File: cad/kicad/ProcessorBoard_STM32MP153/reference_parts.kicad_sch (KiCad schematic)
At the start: 25 parts, among them Q99901 MMBT5551L, Q99902 MMBTA92, SW99901 SW_DIP_x03

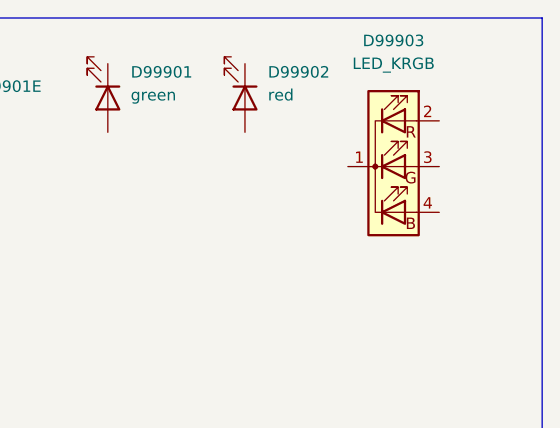
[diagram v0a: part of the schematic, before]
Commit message: double inversion trap
the crab has a double inversion, the pins internal logic is inverted. and the output logic-high is dynamically determined. bruh
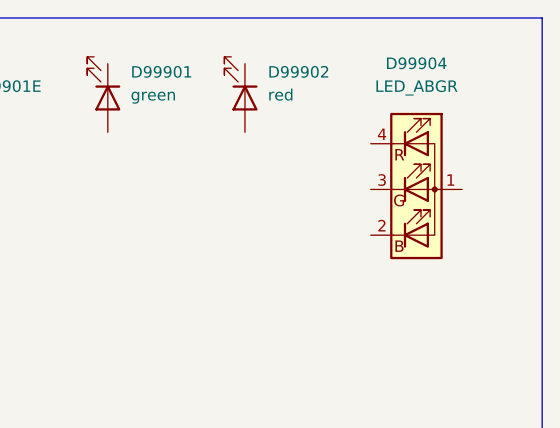
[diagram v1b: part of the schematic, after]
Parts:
- removed D99903: LED_KRGB, LED_SMD:LED_Cree-PLCC4_2x2mm_CW, symbol Device:LED_KRGB
- added D99904: LED_ABGR, symbol Device:LED_ABGR
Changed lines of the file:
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@@
+	)
+	(symbol
+		(lib_id "Device:LED_ABGR")
+		(at 194.31 33.02 0)
+		(unit 1)
+		(body_style 1)
+		(exclude_from_sim no)
+		(in_bom yes)
+		(on_board yes)
+		(in_pos_files yes)
+		(dnp no)
+		(fields_autoplaced yes)
+		(property "Reference" "D99904"
+			(at 194.31 19.05 0)
+			(show_name no)
+			(do_not_autoplace no)
+			(effects
+				(font
+					(size 1.27 1.27)
+				)
+			)
+		)
+		(property "Value" "LED_ABGR"
+			(at 194.31 21.59 0)
+			(show_name no)
+			(do_not_autoplace no)
+			(effects
+				(font
+					(size 1.27 1.27)
+				)
+			)
+		)
+		(property "Footprint" ""
+			(at 194.31 34.29 0)
+			(hide yes)
+			(show_name no)
+			(do_not_autoplace no)
+			(effects
+				(font
+					(size 1.27 1.27)
+				)
+			)
+		)
+		(property "Datasheet" "https://downloads.cree-led.com/files/ds/h/HB-CLMVH-FKA.pdf"
+			(at 194.31 34.29 0)
+			(hide yes)
+			(show_name no)
+			(do_not_autoplace no)
+			(effects
+				(font
+					(size 1.27 1.27)
+				)
+			)
+		)
+		(property "Description" "RGB LED, com-anode, red/green/blue"
+			(at 194.31 33.02 0)
+			(hide yes)
+			(show_name no)
+			(do_not_autoplace no)
+			(effects
+				(font
+					(size 1.27 1.27)
+				)
+			)
+		)
+		(property "mouser" "https://www.mouser.com/en/ProductDetail/Cree-LED/CLMVH-FKA-V3E27C3M2RMG6EB4B3?qs=vcFyY%252BOcAyjw5C6eEBWdHQ%3D%3D"
+			(at 194.31 33.02 0)
+			(hide yes)
+			(show_name no)
+			(do_not_autoplace no)
+			(effects
+				(font
+					(size 1.27 1.27)
+				)
+			)
+		)
+		(property "unit x1" "0.10"
+			(at 194.31 33.02 0)
+			(hide yes)
+			(show_name no)
+			(do_not_autoplace no)
+			(effects
+				(font
+					(size 1.27 1.27)
+				)
+			)
+		)
+		(property "unit x10" "0.007"
+			(at 194.31 33.02 0)
+			(hide yes)
+			(show_name no)
+			(do_not_autoplace no)
+			(effects
+				(font
+					(size 1.27 1.27)
+				)
+			)
+		)
+		(pin "2"
+		)
+		(pin "1"
+		)
+		(pin "4"
+		)
+		(pin "3"
+		)
+		(instances
+			(project "ProcessorBoard_STM32MP153"
+				(path "/e63e39d7-6ac0-4ffd-8aa3-1841a4541b55/157228c5-c462-4e2c-89a8-acc0a1fe94b2"
+					(reference "D99904")
+					(unit 1)
+				)
+			)
+		)
 	)
 	(symbol
@@
 					(unit 1)
 				)
-			)
-		)
-	)
-	(symbol
-		(lib_id "Device:LED_KRGB")
-		(at 191.77 30.48 0)
-		(unit 1)
-		(body_style 1)
-		(exclude_from_sim no)
-		(in_bom yes)
-		(on_board yes)
-		(in_pos_files yes)
-		(dnp no)
-		(fields_autoplaced yes)
-		(property "Reference" "D99903"
-			(at 191.77 16.51 0)
-			(show_name no)
-			(do_not_autoplace no)
-			(effects
-				(font
-					(size 1.27 1.27)
-				)
-			)
-		)
-		(property "Value" "LED_KRGB"
-			(at 191.77 19.05 0)
-			(show_name no)
-			(do_not_autoplace no)
-			(effects
-				(font
-					(size 1.27 1.27)
-				)
-			)
-		)
-		(property "Footprint" "LED_SMD:LED_Cree-PLCC4_2x2mm_CW"
-			(at 191.77 31.75 0)
-			(hide yes)
-			(show_name no)
-			(do_not_autoplace no)
-			(effects
-				(font
-					(size 1.27 1.27)
-				)
-			)
-		)
-		(property "Datasheet" "https://downloads.cree-led.com/files/ds/h/HB-CLMVH-FKA.pdf"
-			(at 191.77 31.75 0)
-			(hide yes)
-			(show_name no)
-			(do_not_autoplace no)
-			(effects
-				(font
-					(size 1.27 1.27)
-				)
-			)
-		)
-		(property "Description" "RGB LED, cathode/red/green/blue"
-			(at 191.77 30.48 0)
-			(hide yes)
-			(show_name no)
-			(do_not_autoplace no)
-			(effects
-				(font
-					(size 1.27 1.27)
-				)
-			)
-		)
-		(property "mouser" "https://www.mouser.com/en/ProductDetail/Cree-LED/CLMVH-FKA-V3E27C3M2RMG6EB4B3?qs=vcFyY%252BOcAyjw5C6eEBWdHQ%3D%3D"
-			(at 191.77 30.48 0)
-			(hide yes)
-			(show_name no)
-			(do_not_autoplace no)
-			(effects
-				(font
-					(size 1.27 1.27)
-				)
-			)
-		)
-		(property "unit x1" "0.10"
-			(at 191.77 30.48 0)
-			(hide yes)
-			(show_name no)
-			(do_not_autoplace no)
-			(effects
-				(font
-					(size 1.27 1.27)
-				)
-			)
-		)
-		(property "unit x10" "0.007"
-			(at 191.77 30.48 0)
-			(hide yes)
-			(show_name no)
-			(do_not_autoplace no)
-			(effects
-				(font
-					(size 1.27 1.27)
-				)
-			)
-		)
-		(pin "1"
-		)
-		(pin "3"
-		)
-		(pin "2"
-		)
-		(pin "4"
-		)
-		(instances
-			(project "ProcessorBoard_STM32MP153"
-				(path "/e63e39d7-6ac0-4ffd-8aa3-1841a4541b55/157228c5-c462-4e2c-89a8-acc0a1fe94b2"
-					(reference "D99903")
-					(unit 1)
-				)

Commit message: all hail the auto router
https://ih1.redbubble.net/image.6083290940.2638/flat,750x,075,f-pad,750x1000,f8f8f8.jpg
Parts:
- C903, C904, C905: footprint Capacitor_SMD:C_01005_0402Metric_Pad0.57x0.30mm_HandSolder -> Capacitor_SMD:C_0402_1005Metric_Pad0.74x0.62mm_HandSolder

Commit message: somewhat fanned
the auto router sucks :( . and the auto fanout sucks. and i routed everything on the wrong grid and it snapped to teh wrong places and i only noticed most of teh way though so i push and make it tomorrows problem
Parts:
- renumbered C901 to C99901, C903 to C99902, C902 to C99903, C904 to C99904, C906 to C99905, C905 to C99906, D99904 to D99903, L901 to L99901, L99901 to L99902, R904 to R99901, R99901 to R99902, R99902 to R99903, R905 to R99904, R99903 to R99905, R901 to R99906, R903 to R99907, R906 to R99908, R99904 to R99909, R907 to R99910
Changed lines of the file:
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@@
 		(dnp no)
 		(fields_autoplaced yes)
-		(property "Reference" "C906"
+		(property "Reference" "C99905"
 			(at 92.71 88.9062 0)
 			(show_name no)
@@
 			(project "ProcessorBoard_STM32MP153"
 				(path "/e63e39d7-6ac0-4ffd-8aa3-1841a4541b55/157228c5-c462-4e2c-89a8-acc0a1fe94b2"
-					(reference "C906")
+					(reference "C99905")
 					(unit 1)
 				)
@@
 		(dnp no)
 		(fields_autoplaced yes)
-		(property "Reference" "R99904"
+		(property "Reference" "R99909"
 			(at 87.63 19.0499 0)
 			(show_name no)
@@
 			(project "ProcessorBoard_STM32MP153"
 				(path "/e63e39d7-6ac0-4ffd-8aa3-1841a4541b55/157228c5-c462-4e2c-89a8-acc0a1fe94b2"
-					(reference "R99904")
+					(reference "R99909")
 					(unit 1)
 				)
@@
 		(dnp no)
 		(fields_autoplaced yes)
-		(property "Reference" "R99901"
+		(property "Reference" "R99902"
 			(at 21.59 19.0499 0)
 			(show_name no)
@@
 			(project "ProcessorBoard_STM32MP153"
 				(path "/e63e39d7-6ac0-4ffd-8aa3-1841a4541b55/157228c5-c462-4e2c-89a8-acc0a1fe94b2"
-					(reference "R99901")
+					(reference "R99902")
 					(unit 1)
 				)
@@
 		(dnp no)
 		(fields_autoplaced yes)
-		(property "Reference" "R901"
+		(property "Reference" "R99906"
 			(at 55.88 19.0499 0)
 			(show_name no)
@@
 			(project "ProcessorBoard_STM32MP153"
 				(path "/e63e39d7-6ac0-4ffd-8aa3-1841a4541b55/157228c5-c462-4e2c-89a8-acc0a1fe94b2"
-					(reference "R901")
+					(reference "R99906")
 					(unit 1)
 				)
@@
 		(dnp no)
 		(fields_autoplaced yes)
-		(property "Reference" "C904"
+		(property "Reference" "C99904"
 			(at 82.55 88.9062 0)
 			(show_name no)
@@
 			(project "ProcessorBoard_STM32MP153"
 				(path "/e63e39d7-6ac0-4ffd-8aa3-1841a4541b55/157228c5-c462-4e2c-89a8-acc0a1fe94b2"
-					(reference "C904")
+					(reference "C99904")
 					(unit 1)
 				)
@@
 		(dnp no)
 		(fields_autoplaced yes)
-		(property "Reference" "L901"
+		(property "Reference" "L99901"
 			(at 20.32 121.9199 0)
 			(show_name no)
@@
 			(project "ProcessorBoard_STM32MP153"
 				(path "/e63e39d7-6ac0-4ffd-8aa3-1841a4541b55/157228c5-c462-4e2c-89a8-acc0a1fe94b2"
-					(reference "L901")
+					(reference "L99901")
 					(unit 1)
 				)
@@
 		(dnp no)
 		(fields_autoplaced yes)
-		(property "Reference" "C905"
+		(property "Reference" "C99906"
 			(at 102.87 88.9062 0)
 			(show_name no)
@@
 			(project "ProcessorBoard_STM32MP153"
 				(path "/e63e39d7-6ac0-4ffd-8aa3-1841a4541b55/157228c5-c462-4e2c-89a8-acc0a1fe94b2"
-					(reference "C905")
+					(reference "C99906")
 					(unit 1)
 				)
@@
 		(dnp no)
 		(fields_autoplaced yes)
-		(property "Reference" "D99904"
+		(property "Reference" "D99903"
 			(at 194.31 19.05 0)
 			(show_name no)
@@
 			(project "ProcessorBoard_STM32MP153"
 				(path "/e63e39d7-6ac0-4ffd-8aa3-1841a4541b55/157228c5-c462-4e2c-89a8-acc0a1fe94b2"
-					(reference "D99904")
+					(reference "D99903")
 					(unit 1)
 				)
@@
 		(dnp no)
 		(fields_autoplaced yes)
-		(property "Reference" "R906"
+		(property "Reference" "R99908"
 			(at 76.2 19.0499 0)
 			(show_name no)
@@
 			(project "ProcessorBoard_STM32MP153"
 				(path "/e63e39d7-6ac0-4ffd-8aa3-1841a4541b55/157228c5-c462-4e2c-89a8-acc0a1fe94b2"
-					(reference "R906")
+					(reference "R99908")
 					(unit 1)
 				)
@@
 		(dnp no)
 		(fields_autoplaced yes)
-		(property "Reference" "C903"
+		(property "Reference" "C99902"
 			(at 34.29 87.6362 0)
 			(show_name no)
@@
 			(project "ProcessorBoard_STM32MP153"
 				(path "/e63e39d7-6ac0-4ffd-8aa3-1841a4541b55/157228c5-c462-4e2c-89a8-acc0a1fe94b2"
-					(reference "C903")
+					(reference "C99902")
 					(unit 1)
 				)
@@
 		(dnp no)
 		(fields_autoplaced yes)
-		(property "Reference" "R904"
+		(property "Reference" "R99901"
 			(at 20.32 68.5799 0)
 			(show_name no)
@@
 			(project "ProcessorBoard_STM32MP153"
 				(path "/e63e39d7-6ac0-4ffd-8aa3-1841a4541b55/157228c5-c462-4e2c-89a8-acc0a1fe94b2"
-					(reference "R904")
+					(reference "R99901")
 					(unit 1)
 				)
@@
 		(dnp no)
 		(fields_autoplaced yes)
-		(property "Reference" "C901"
+		(property "Reference" "C99901"
 			(at 21.59 87.6362 0)
 			(show_name no)
@@
 			(project "ProcessorBoard_STM32MP153"
 				(path "/e63e39d7-6ac0-4ffd-8aa3-1841a4541b55/157228c5-c462-4e2c-89a8-acc0a1fe94b2"
-					(reference "C901")
+					(reference "C99901")
 					(unit 1)
 				)
@@
 		(dnp no)
 		(fields_autoplaced yes)
-		(property "Reference" "R903"
+		(property "Reference" "R99907"
 			(at 66.04 19.0499 0)
 			(show_name no)
@@
 			(project "ProcessorBoard_STM32MP153"
 				(path "/e63e39d7-6ac0-4ffd-8aa3-1841a4541b55/157228c5-c462-4e2c-89a8-acc0a1fe94b2"
-					(reference "R903")
+					(reference "R99907")
 					(unit 1)
 				)
@@
 		(dnp no)
 		(fields_autoplaced yes)
-		(property "Reference" "R99903"
+		(property "Reference" "R99905"
 			(at 44.45 19.0499 0)
 			(show_name no)
@@
 			(project "ProcessorBoard_STM32MP153"
 				(path "/e63e39d7-6ac0-4ffd-8aa3-1841a4541b55/157228c5-c462-4e2c-89a8-acc0a1fe94b2"
-					(reference "R99903")
+					(reference "R99905")
 					(unit 1)
 				)
@@
 		(dnp no)
 		(fields_autoplaced yes)
-		(property "Reference" "L99901"
+		(property "Reference" "L99902"
 			(at 29.21 121.9199 0)
 			(show_name no)
@@
 			(project "ProcessorBoard_STM32MP153"
 				(path "/e63e39d7-6ac0-4ffd-8aa3-1841a4541b55/157228c5-c462-4e2c-89a8-acc0a1fe94b2"
-					(reference "L99901")
+					(reference "L99902")
 					(unit 1)
 				)
@@
 		(dnp no)
 		(fields_autoplaced yes)
-		(property "Reference" "R905"
+		(property "Reference" "R99904"
 			(at 34.29 19.0499 0)
 			(show_name no)
@@
 			(project "ProcessorBoard_STM32MP153"
 				(path "/e63e39d7-6ac0-4ffd-8aa3-1841a4541b55/157228c5-c462-4e2c-89a8-acc0a1fe94b2"
-					(reference "R905")
+					(reference "R99904")
 					(unit 1)
 				)
@@
 		(dnp no)
 		(fields_autoplaced yes)
-		(property "Reference" "R907"
+		(property "Reference" "R99910"
 			(at 100.33 19.0499 0)
 			(show_name no)
@@
 			(project "ProcessorBoard_STM32MP153"
 				(path "/e63e39d7-6ac0-4ffd-8aa3-1841a4541b55/157228c5-c462-4e2c-89a8-acc0a1fe94b2"
-					(reference "R907")
+					(reference "R99910")
 					(unit 1)
 				)
@@
 		(dnp no)
 		(fields_autoplaced yes)
-		(property "Reference" "R99902"
+		(property "Reference" "R99903"
 			(at 21.59 27.9399 0)
 			(show_name no)
@@
 			(project "ProcessorBoard_STM32MP153"
 				(path "/e63e39d7-6ac0-4ffd-8aa3-1841a4541b55/157228c5-c462-4e2c-89a8-acc0a1fe94b2"
-					(reference "R99902")
+					(reference "R99903")
 					(unit 1)
 				)
@@
 		(dnp no)
 		(fields_autoplaced yes)
-		(property "Reference" "C902"
+		(property "Reference" "C99903"
 			(at 71.12 88.9062 0)
 			(show_name no)
@@
 			(project "ProcessorBoard_STM32MP153"
 				(path "/e63e39d7-6ac0-4ffd-8aa3-1841a4541b55/157228c5-c462-4e2c-89a8-acc0a1fe94b2"
-					(reference "C902")
+					(reference "C99903")
 					(unit 1)
 				)

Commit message: boo womp 10000
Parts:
- added L99903: 1u, Inductor_SMD:L_0805_2012Metric_Pad1.05x1.20mm_HandSolder, symbol Device:L_Small
- added R99911: 2.49k, Resistor_SMD:R_0603_1608Metric_Pad0.98x0.95mm_HandSolder, symbol Device:R_Small_US
- added R99912: 0, Resistor_SMD:R_0603_1608Metric, symbol Device:R_Small_US
- D99903: footprint (none) -> LED_SMD:LED_ASMB-KTF0-0A306
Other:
- moved on the sheet: L99901, L99902, R99907, R99908, R99909, R99910

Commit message: i forgor track spacing :(
need to redo ddr
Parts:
- added R99913: 22, Resistor_SMD:R_0603_1608Metric, symbol Device:R_Small_US
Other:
- moved on the sheet: R99912
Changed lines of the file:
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@@
 	)
 	(symbol
+		(lib_id "Device:R_Small_US")
+		(at 31.75 69.85 0)
+		(unit 1)
+		(body_style 1)
+		(exclude_from_sim no)
+		(in_bom no)
+		(on_board yes)
+		(in_pos_files yes)
+		(dnp no)
+		(fields_autoplaced yes)
+		(property "Reference" "R99913"
+			(at 34.29 68.5799 0)
+			(show_name no)
+			(do_not_autoplace no)
+			(effects
+				(font
+					(size 1.27 1.27)
+				)
+				(justify left)
+			)
+		)
+		(property "Value" "22"
+			(at 34.29 71.1199 0)
+			(show_name no)
+			(do_not_autoplace no)
+			(effects
+				(font
+					(size 1.27 1.27)
+				)
+				(justify left)
+			)
+		)
+		(property "Footprint" "Resistor_SMD:R_0603_1608Metric"
+			(at 31.75 69.85 0)
+			(hide yes)
+			(show_name no)
+			(do_not_autoplace no)
+			(effects
+				(font
+					(size 1.27 1.27)
+				)
+			)
+		)
+		(property "Datasheet" ""
+			(at 31.75 69.85 0)
+			(hide yes)
+			(show_name no)
+			(do_not_autoplace no)
+			(effects
+				(font
+					(size 1.27 1.27)
+				)
+			)
+		)
+		(property "Description" "22R, 0.5%, 50ppm, 100mW, 75V, +155C"
+			(at 31.75 69.85 0)
+			(hide yes)
+			(show_name no)
+			(do_not_autoplace no)
+			(effects
+				(font
+					(size 1.27 1.27)
+				)
+			)
+		)
+		(property "mouser" "https://www.mouser.com/en/ProductDetail/YAGEO/RT0603DRE0722RL?qs=sGAEpiMZZMvdGkrng054t98Xz4DA4UW4aVwvkunzeD8%3D"
+			(at 31.75 69.85 0)
+			(hide yes)
+			(show_name no)
+			(do_not_autoplace no)
+			(effects
+				(font
+					(size 1.27 1.27)
+				)
+			)
+		)
+		(property "unit x1" "0.10"
+			(at 31.75 69.85 0)
+			(hide yes)
+			(show_name no)
+			(do_not_autoplace no)
+			(effects
+				(font
+					(size 1.27 1.27)
+				)
+			)
+		)
+		(property "unit x10" "0.018"
+			(at 31.75 69.85 0)
+			(hide yes)
+			(show_name no)
+			(do_not_autoplace no)
+			(effects
+				(font
+					(size 1.27 1.27)
+				)
+			)
+		)
+		(pin "2"
+		)
+		(pin "1"
+		)
+		(instances
+			(project "ProcessorBoard_STM32MP153"
+				(path "/e63e39d7-6ac0-4ffd-8aa3-1841a4541b55/157228c5-c462-4e2c-89a8-acc0a1fe94b2"
+					(reference "R99913")
+					(unit 1)
+				)
+			)
+		)
+	)
+	(symbol
 		(lib_id "Device:C_Small")
 		(at 80.01 90.17 0)
@@
 	(symbol
 		(lib_id "Device:R_Small_US")
-		(at 30.48 69.85 0)
+		(at 44.45 69.85 0)
 		(unit 1)
 		(body_style 1)
@@
 		(fields_autoplaced yes)
 		(property "Reference" "R99912"
-			(at 33.02 68.5799 0)
+			(at 46.99 68.5799 0)
 			(show_name no)
 			(do_not_autoplace no)
@@
 		)
 		(property "Value" "0"
-			(at 33.02 71.1199 0)
+			(at 46.99 71.1199 0)
 			(show_name no)
 			(do_not_autoplace no)
@@
 		)
 		(property "Footprint" "Resistor_SMD:R_0603_1608Metric"
-			(at 30.48 69.85 0)
+			(at 44.45 69.85 0)
 			(hide yes)
 			(show_name no)
@@
 		)
 		(property "Datasheet" ""
-			(at 30.48 69.85 0)
+			(at 44.45 69.85 0)
 			(hide yes)
 			(show_name no)
@@
 		)
 		(property "Description" "jumper"
-			(at 30.48 69.85 0)
+			(at 44.45 69.85 0)
 			(hide yes)
 			(show_name no)

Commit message: shuffled core back to left side of board, fits better
row row the power planes under mpu
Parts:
- added C99907: 10u, Capacitor_SMD:C_0805_2012Metric_Pad1.18x1.45mm_HandSolder, symbol Device:C_Polarized_Small_US
- R99912: footprint Resistor_SMD:R_0603_1608Metric -> Resistor_SMD:R_0402_1005Metric_Pad0.72x0.64mm_HandSolder
- R99913: footprint Resistor_SMD:R_0603_1608Metric -> Resistor_SMD:R_0402_1005Metric_Pad0.72x0.64mm_HandSolder; mouser https://www.mouser.com/en/ProductDetail/YAGEO/RT0603DRE0722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 -> https://www.mouser.com/en/ProductDetail/Vishay/CRCW040222R0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; unit x10 0.018 -> 0.02; now in the parts list
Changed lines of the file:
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@@
 		(body_style 1)
 		(exclude_from_sim no)
-		(in_bom no)
+		(in_bom yes)
 		(on_board yes)
 		(in_pos_files yes)
@@
 			)
 		)
-		(property "Footprint" "Resistor_SMD:R_0603_1608Metric"
+		(property "Footprint" "Resistor_SMD:R_0402_1005Metric_Pad0.72x0.64mm_HandSolder"
 			(at 31.75 69.85 0)
 			(hide yes)
@@
 			)
 		)
-		(property "Description" "22R, 0.5%, 50ppm, 100mW, 75V, +155C"
+		(property "Description" "22R, 1%, 100mW, 100ppm, 75V, +155C"
 			(at 31.75 69.85 0)
 			(hide yes)
@@
 			)
 		)
-		(property "mouser" "https://www.mouser.com/en/ProductDetail/YAGEO/RT0603DRE0722RL?qs=sGAEpiMZZMvdGkrng054t98Xz4DA4UW4aVwvkunzeD8%3D"
+		(property "mouser" "https://www.mouser.com/en/ProductDetail/Vishay/CRCW040222R0FKED?qs=sGAEpiMZZMvdGkrng054txEw7b1YnvGuyQ7ZYbf%2FtI4%3D"
 			(at 31.75 69.85 0)
 			(hide yes)
@@
 			)
 		)
-		(property "unit x10" "0.018"
+		(property "unit x10" "0.02"
 			(at 31.75 69.85 0)
 			(hide yes)
@@
 	)
 	(symbol
+		(lib_id "Device:C_Polarized_Small_US")
+		(at 59.69 69.85 0)
+		(unit 1)
+		(body_style 1)
+		(exclude_from_sim no)
+		(in_bom yes)
+		(on_board yes)
+		(in_pos_files yes)
+		(dnp no)
+		(fields_autoplaced yes)
+		(property "Reference" "C99907"
+			(at 62.23 68.1481 0)
+			(show_name no)
+			(do_not_autoplace no)
+			(effects
+				(font
+					(size 1.27 1.27)
+				)
+				(justify left)
+			)
+		)
+		(property "Value" "10u"
+			(at 62.23 70.6881 0)
+			(show_name no)
+			(do_not_autoplace no)
+			(effects
+				(font
+					(size 1.27 1.27)
+				)
+				(justify left)
+			)
+		)
+		(property "Footprint" "Capacitor_SMD:C_0805_2012Metric_Pad1.18x1.45mm_HandSolder"
+			(at 59.69 69.85 0)
+			(hide yes)
+			(show_name no)
+			(do_not_autoplace no)
+			(effects
+				(font
+					(size 1.27 1.27)
+				)
+			)
+		)
+		(property "Datasheet" ""
+			(at 59.69 69.85 0)
+			(hide yes)
+			(show_name no)
+			(do_not_autoplace no)
+			(effects
+				(font
+					(size 1.27 1.27)
+				)
+			)
+		)
+		(property "Description" "10uF, 10Vdc, 5.9R, 10%, +125C"
+			(at 59.69 69.85 0)
+			(hide yes)
+			(show_name no)
+			(do_not_autoplace no)
+			(effects
+				(font
+					(size 1.27 1.27)
+				)
+			)
+		)
+		(property "vendor" "https://www.mouser.com/en/ProductDetail/Vishay-Sprague/TMCP1A106KTRF?qs=sGAEpiMZZMsh%252B1woXyUXj%252Bp8lp8l%2FqQ27sYKu53jFUE%3D"
+			(at 59.69 69.85 0)
+			(hide yes)
+			(show_name no)
+			(do_not_autoplace no)
+			(effects
+				(font
+					(size 1.27 1.27)
+				)
+			)
+		)
+		(property "unit x1" "0.38"
+			(at 59.69 69.85 0)
+			(hide yes)
+			(show_name no)
+			(do_not_autoplace no)
+			(effects
+				(font
+					(size 1.27 1.27)
+				)
+			)
+		)
+		(property "unit x10" "0.164"
+			(at 59.69 69.85 0)
+			(hide yes)
+			(show_name no)
+			(do_not_autoplace no)
+			(effects
+				(font
+					(size 1.27 1.27)
+				)
+			)
+		)
+		(pin "2"
+		)
+		(pin "1"
+		)
+		(instances
+			(project "ProcessorBoard_STM32MP153"
+				(path "/e63e39d7-6ac0-4ffd-8aa3-1841a4541b55/157228c5-c462-4e2c-89a8-acc0a1fe94b2"
+					(reference "C99907")
+					(unit 1)
+				)
+			)
+		)
+	)
+	(symbol
 		(lib_id "Device:C_Small")
 		(at 19.05 88.9 0)
@@
 			)
 		)
-		(property "Footprint" "Resistor_SMD:R_0603_1608Metric"
+		(property "Footprint" "Resistor_SMD:R_0402_1005Metric_Pad0.72x0.64mm_HandSolder"
 			(at 44.45 69.85 0)
 			(hide yes)
